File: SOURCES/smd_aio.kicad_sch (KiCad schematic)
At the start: 71 parts, among them J1 RCA_01, J2 RCA_01, P1 MUTE, P16 TST, P2 CONN_01X04, P23 TST, P3 CONN_01X03, P32 /SD, P33 GP4, P34 GP5, P35 GP6, P4 CONN_02X05 Boxed, P5 STDCONN, P6 CONN_02X04, P7 CONN_02X04, P8 CONN_02X04, SW1 SW_PUSH, U1 ADAU1701, U2 24AA256SN, U3 SN74LVC14ADG4, U8 MCP23008-xSS

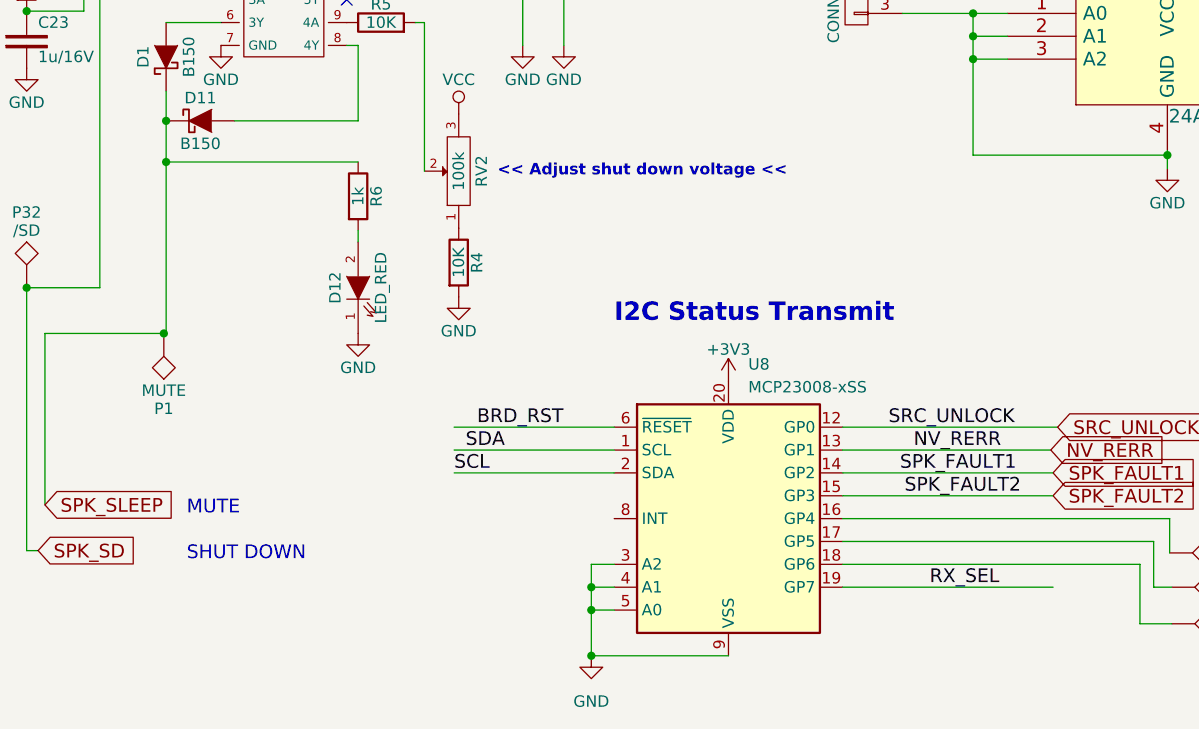
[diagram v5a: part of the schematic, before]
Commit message: Added mute adjust, improved layout.
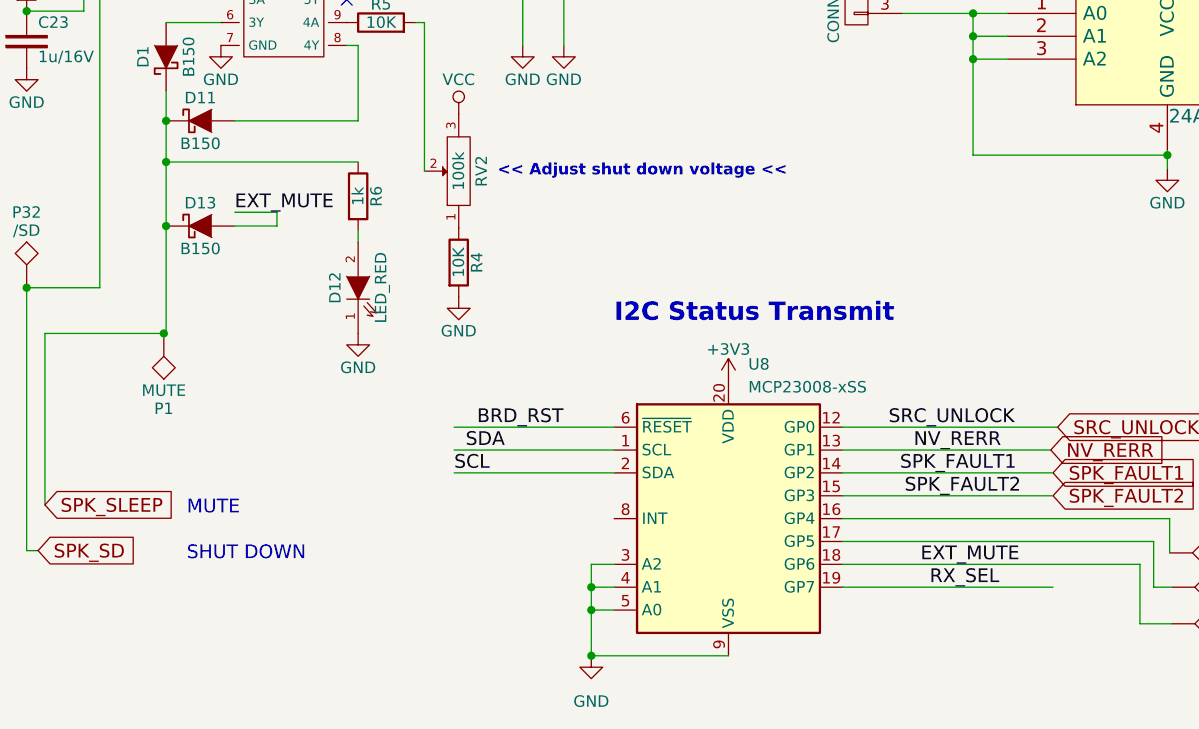
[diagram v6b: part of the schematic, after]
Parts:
- added D13: B150, fdsp_diode:SMA, symbol smd_aio-rescue:D_Schottky
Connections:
- net SPK_SLEEP: now also D13.1 (K)
- net EXT_MUTE: now reaches P35.1, U8.18 (GP6)
- net EXT_MUTE: now also D13.2 (A)
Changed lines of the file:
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@@
   (junction (at 143.256 144.272) (diameter 0) (color 0 0 0 0)
   )
+  (junction (at 39.116 212.598) (diameter 0) (color 0 0 0 0)
+  )
   (junction (at 112.014 39.878) (diameter 0) (color 0 0 0 0)
   )
@@
     (stroke (width 0) (type default))
   )
+  (wire (pts (xy 51.435 211.074) (xy 51.435 212.598))
+    (stroke (width 0) (type default))
+  )
   (wire (pts (xy 150.622 245.11) (xy 150.622 248.92))
     (stroke (width 0) (type default))
@@
     (stroke (width 0) (type default))
   )
+  (wire (pts (xy 51.435 211.074) (xy 46.736 211.074))
+    (stroke (width 0) (type default))
+  )
   (wire (pts (xy 134.366 116.078) (xy 134.366 114.808))
     (stroke (width 0) (type default))
@@
     (stroke (width 0) (type default))
   )
-  (wire (pts (xy 39.116 224.536) (xy 39.116 205.486))
+  (wire (pts (xy 39.116 224.536) (xy 39.116 212.598))
     (stroke (width 0) (type default))
   )
@@
     (stroke (width 0) (type default))
   )
+  (wire (pts (xy 39.116 212.598) (xy 39.116 205.486))
+    (stroke (width 0) (type default))
+  )
   (wire (pts (xy 164.084 94.488) (xy 164.084 94.996))
     (stroke (width 0) (type default))
@@
     (stroke (width 0) (type default))
   )
+  (wire (pts (xy 51.435 212.598) (xy 46.736 212.598))
+    (stroke (width 0) (type default))
+  )
   (wire (pts (xy 195.58 151.892) (xy 198.374 151.892))
     (stroke (width 0) (type default))
@@
     (effects (font (size 1.524 1.524)) (justify left bottom))
   )
+  (label "EXT_MUTE" (at 122.936 250.19 0) (fields_autoplaced)
+    (effects (font (size 1.524 1.524)) (justify left bottom))
+  )
   (label "SPK_FAULT2" (at 121.158 242.57 0) (fields_autoplaced)
     (effects (font (size 1.524 1.524)) (justify left bottom))
@@
     (effects (font (size 1.524 1.524)) (justify left bottom))
   )
+  (label "EXT_MUTE" (at 46.736 211.074 0) (fields_autoplaced)
+    (effects (font (size 1.524 1.524)) (justify left bottom))
+  )
   (global_label "MP9" (shape output) (at 67.31 81.534 180)
     (effects (font (size 1.3208 1.3208)) (justify right))
@@
       (effects (font (size 1.27 1.27)) hide)
     )
-    (pin "2")
     (pin "1")
+    (pin "2")
     (instances
       (project "smd_aio"
@@
       (effects (font (size 1.27 1.27)) hide)
     )
-    (pin "12")
-    (pin "20")
-    (pin "9")
-    (pin "4")
-    (pin "3")
-    (pin "5")
-    (pin "8")
-    (pin "7")
-    (pin "11")
-    (pin "6")
+    (pin "1")
     (pin "10")
-    (pin "15")
+    (pin "11")
+    (pin "12")
     (pin "13")
     (pin "14")
+    (pin "15")
     (pin "16")
     (pin "17")
@@
     (pin "19")
     (pin "2")
-    (pin "1")
+    (pin "20")
+    (pin "3")
+    (pin "4")
+    (pin "5")
+    (pin "6")
+    (pin "7")
+    (pin "8")
+    (pin "9")
     (instances
       (project "smd_aio"
@@
         )
       )
+    )
+  )
+  (symbol (lib_id "smd_aio-rescue:D_Schottky") (at 42.926 212.598 0) (unit 1)
+    (in_bom yes) (on_board yes) (dnp no)
+    (property "Reference" "D13" (at 42.926 210.058 0)
+      (effects (font (size 1.27 1.27)))
+    )
+    (property "Value" "B150" (at 42.926 215.138 0)
+      (effects (font (size 1.27 1.27)))
+    )
+    (property "Footprint" "fdsp_diode:SMA" (at 42.926 212.598 0)
+      (effects (font (size 1.27 1.27)) hide)
+    )
+    (property "Datasheet" "" (at 42.926 212.598 0)
+      (effects (font (size 1.27 1.27)) hide)
+    )
+    (pin "1")
+    (pin "2")
+    (instances
+      (project "smd_aio"
+        (path "/4c49a07c-9ad4-4758-901a-e68e360dc17d"
+          (reference "D13") (unit 1)
+        )
+      )

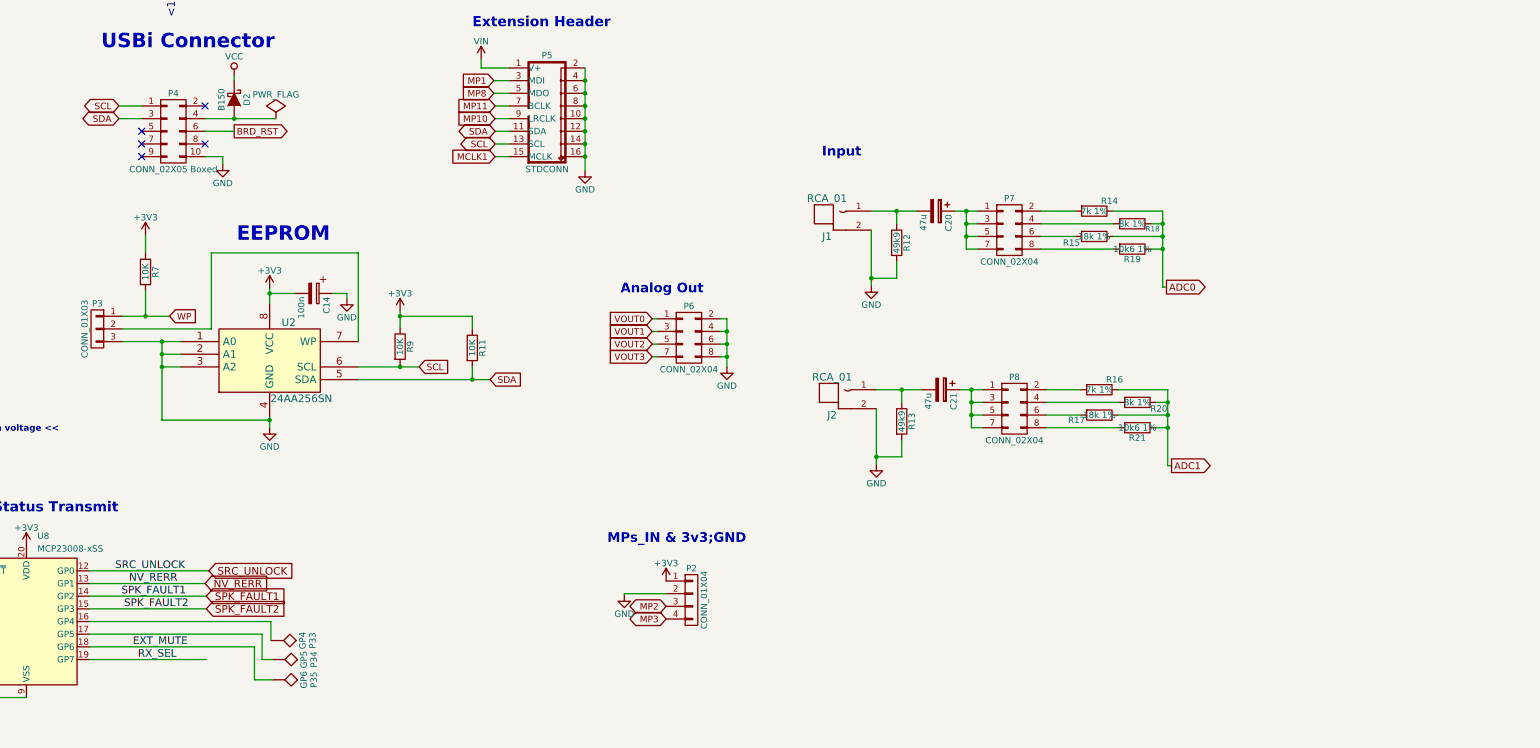
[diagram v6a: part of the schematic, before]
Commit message: Added HP amp
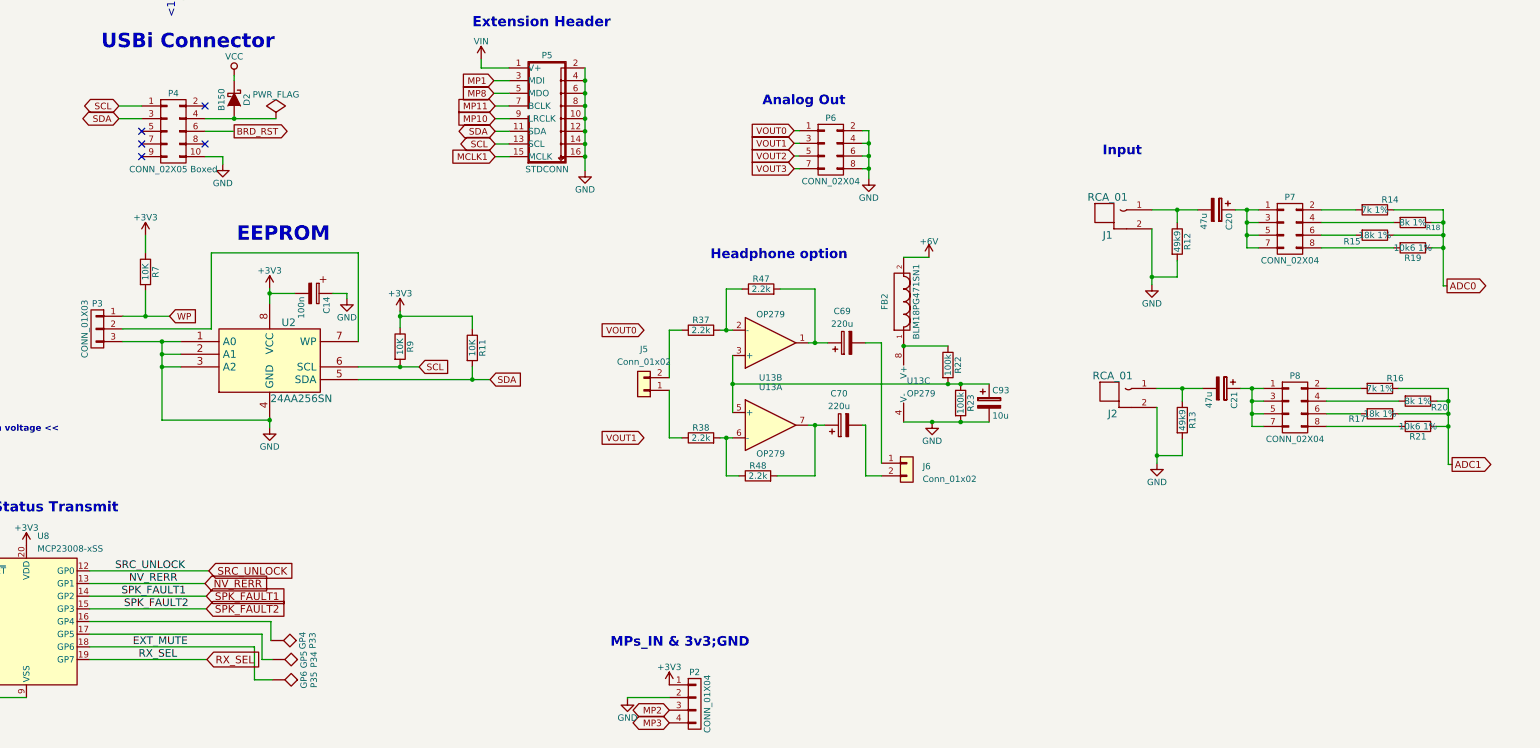
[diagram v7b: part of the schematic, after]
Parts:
- added C69, C70: 220u, Capacitor_SMD:CP_Elec_6.3x5.9, symbol Device:C_Polarized
- added C93: 10u, fdsp_capacitor:C_Radial_D5_L11_P2, symbol smd_aio-rescue:CP
- added FB2: BLM18PG471SN1, fdsp_resistor:R_0603_HandSoldering, symbol smd_aio-rescue:FILTER
- added J5, J6: Conn_01x02, Connector_PinHeader_2.54mm:PinHeader_1x02_P2.54mm_Vertical, symbol Connector_Generic:Conn_01x02
- added R22, R23: 100k, fdsp_resistor:R_0603_HandSoldering, symbol smd_aio-rescue:R
- added R37, R38, R47, R48: 2.2k, fdsp_resistor:R_0603_HandSoldering, symbol smd_aio-rescue:R
- added U13: OP279, Package_SO:SO-8_3.9x4.9mm_P1.27mm, symbol Amplifier_Operational:OP279
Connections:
- net GND: now also C93.2, R23.2, U13.4 (V-)
- new net: C69.1, R47.2, U13.1
- new net: C69.2, J6.1 (Pin_1)
- new net: R37.2, R47.1, U13.2 (-)
- new net: C93.1, R22.2, R23.1, U13.3 (+), U13.5 (+)
- new net: R38.2, R48.1, U13.6 (-)
- new net: C70.1, R48.2, U13.7
- new net: J5.1 (Pin_1), R38.1
- new net: J5.2 (Pin_2), R37.1
- new net: C70.2, J6.2 (Pin_2)
- new net: FB2.1, R22.1, U13.8 (V+)
- new net +6V: FB2.2
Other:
- note added: "Headphone option"
- moved on the sheet: C20, C21, J1, J2, P2, P6, P7, P8, R12, R13, R14, R15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

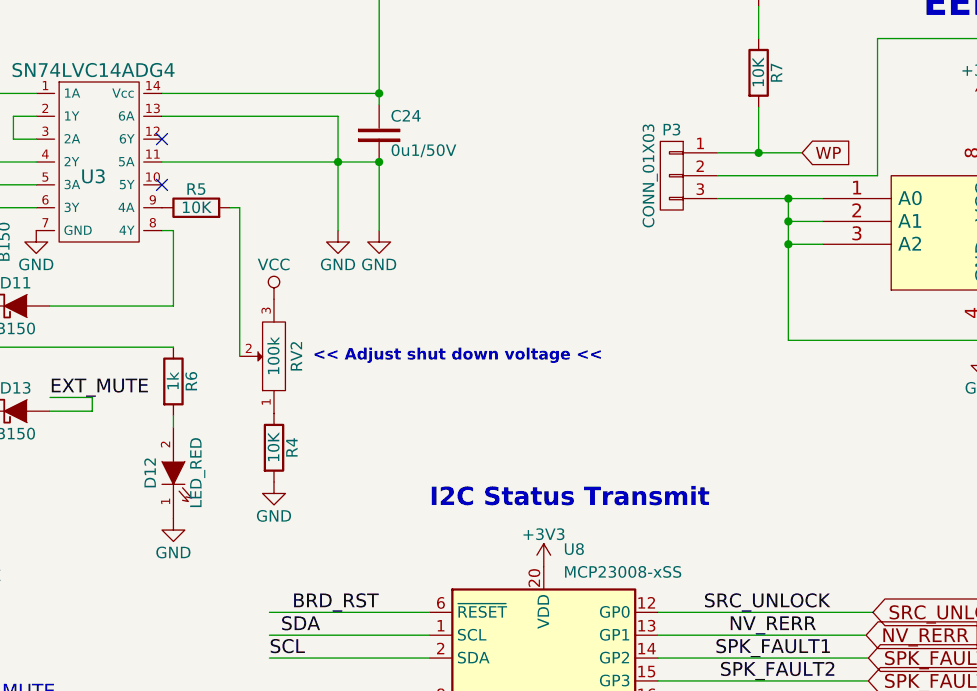
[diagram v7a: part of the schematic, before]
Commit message: Added BAT54s OV protect.
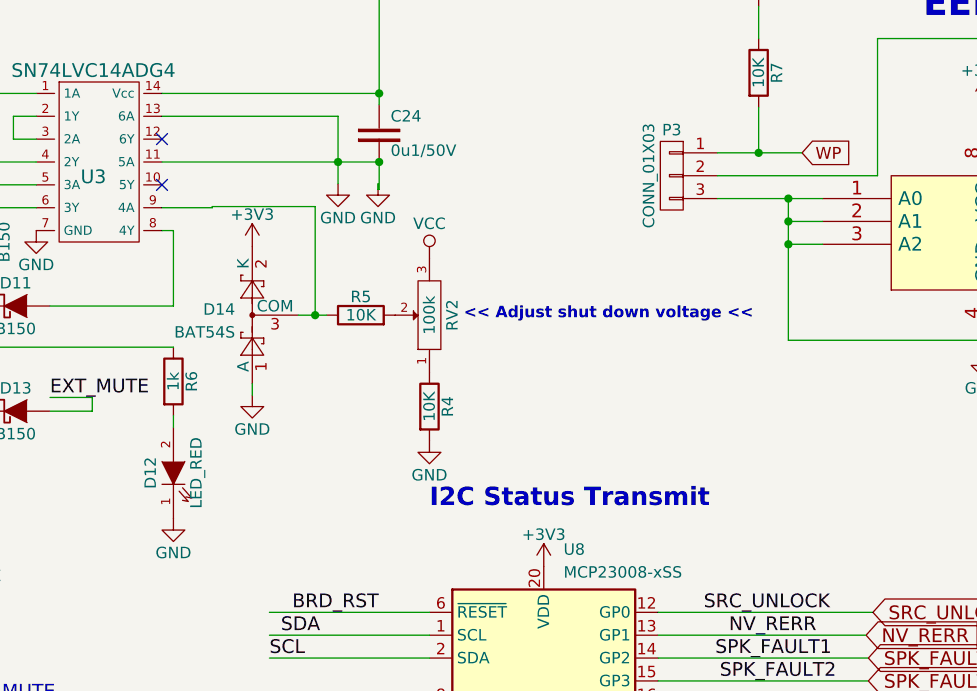
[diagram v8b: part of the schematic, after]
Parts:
- added D14: BAT54S, Package_TO_SOT_SMD:SOT-23, symbol Diode:BAT54S
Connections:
- net +3V3: now also D14.2 (K)
- net GND: now also D14.1 (A)
- net at R5.1, U3.9 (4A): now also D14.3 (COM)
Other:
- moved on the sheet: R4, R5, RV2
